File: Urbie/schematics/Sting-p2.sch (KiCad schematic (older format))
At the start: 12 parts

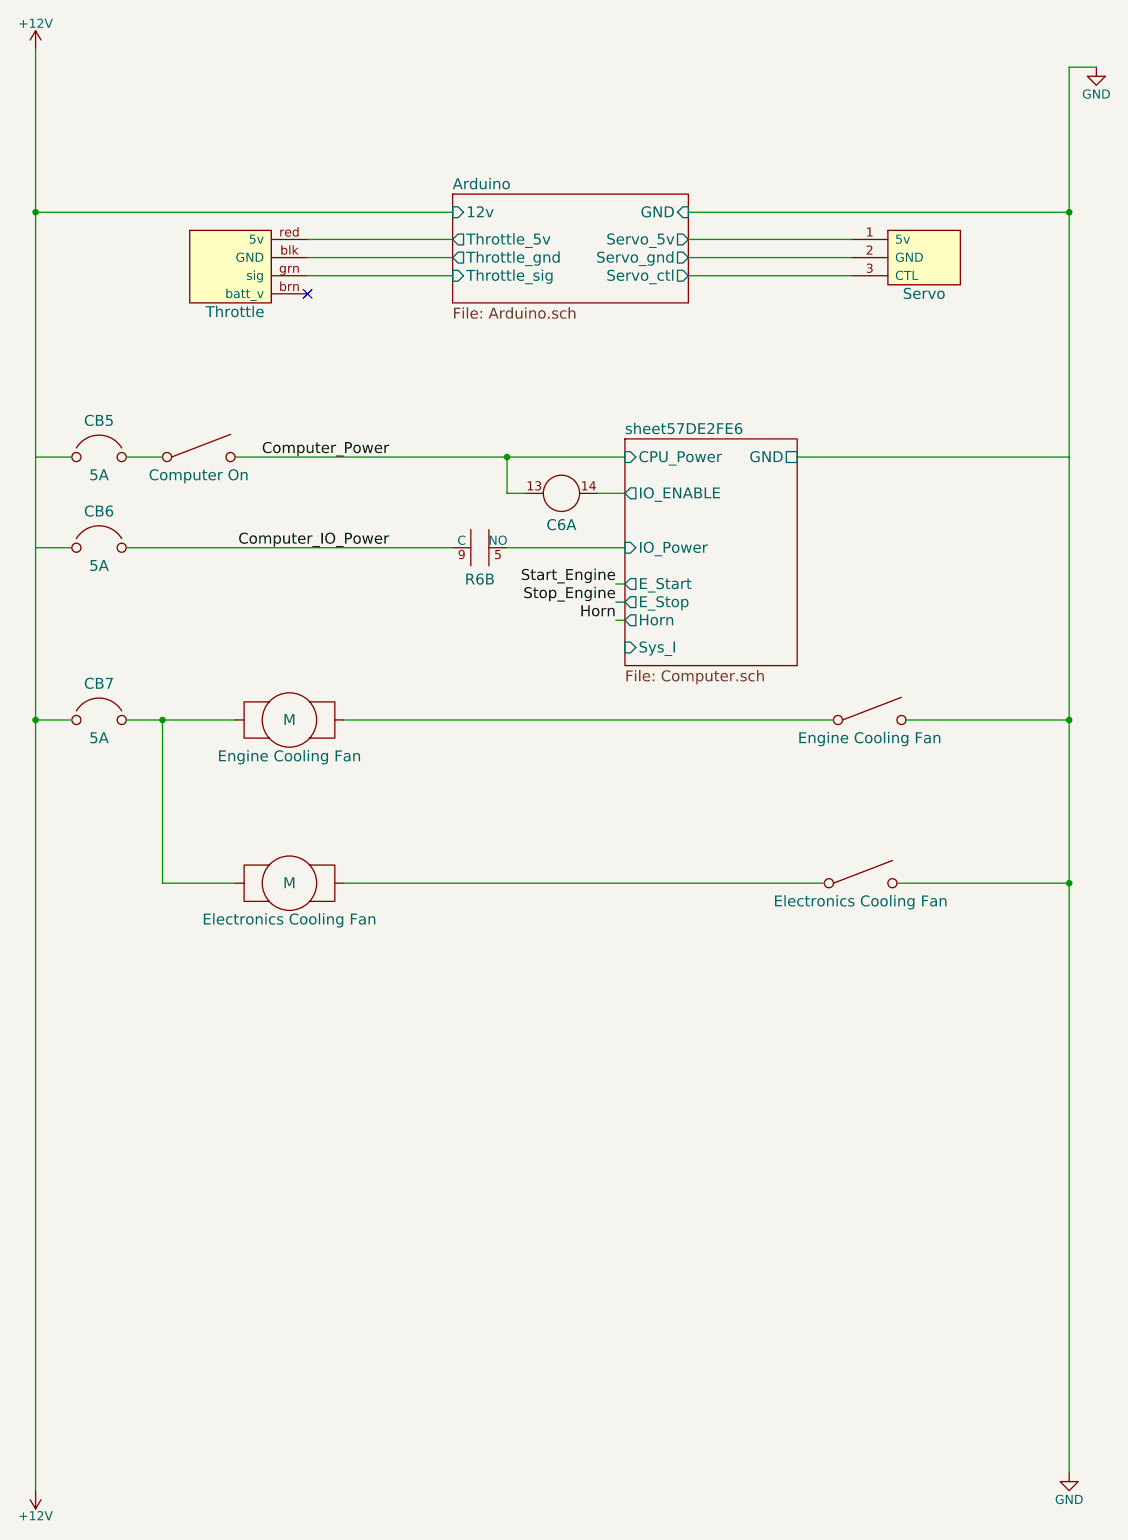
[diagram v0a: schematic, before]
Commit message: added DPDT switch for Hazard lights on Urbie
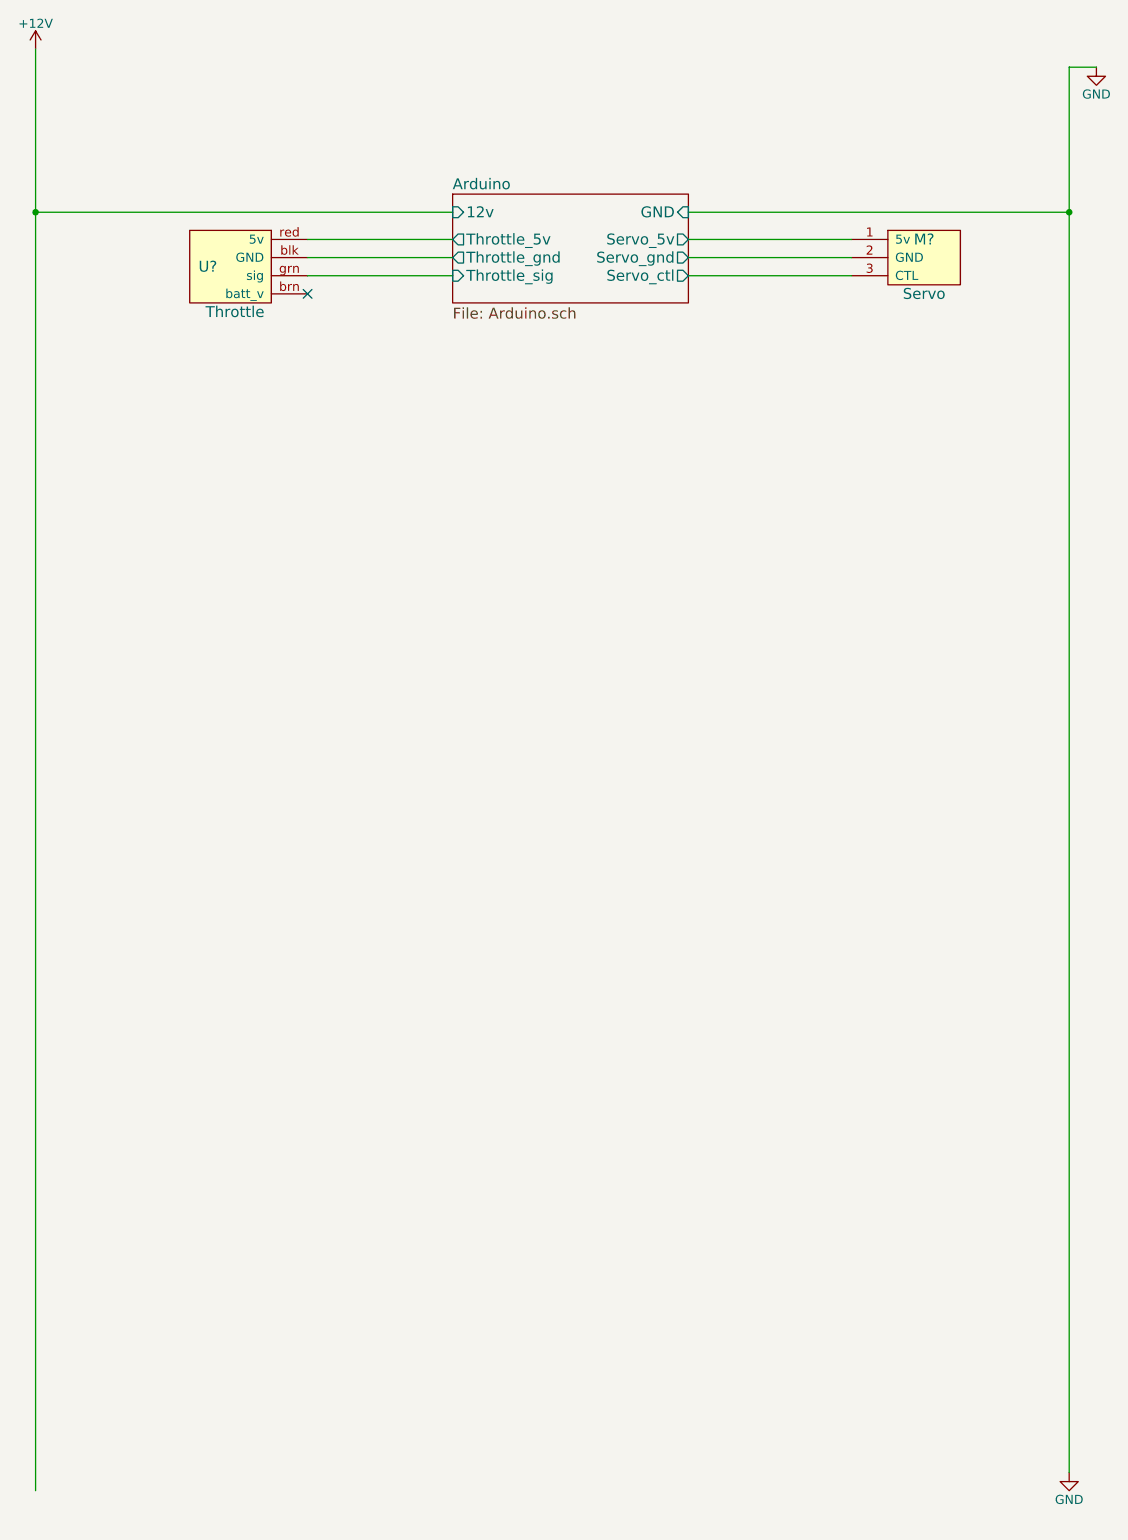
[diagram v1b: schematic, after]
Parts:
- removed C6, R6: CR, symbol CR
- removed CB5, CB6, CB7: 5A, symbol CB
- removed M: Engine Cooling Fan, symbol Motor
- removed M: Electronics Cooling Fan, symbol Motor
- removed SW?: Computer On, symbol SW_SPST
- removed SW?: Engine Cooling Fan, symbol SW_SPST
- removed SW?: Electronics Cooling Fan, symbol SW_SPST
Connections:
- net labels removed: Computer_IO_Power, Computer_Power, Horn, Start_Engine, Stop_Engine
- wire segments 32 -> 11
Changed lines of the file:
@@
 EESchema Schematic File Version 2
+LIBS:UrbieSchematics-rescue
 LIBS:power
 LIBS:device
@@
 $Descr USLetter 8500 11000 portrait
 encoding utf-8
-Sheet 3 6
-Title "Urbie - Gasoline Urban Concept"
-Date "2016-11-19"
-Rev "1.2"
+Sheet 4 5
+Title "Sting - Gasoline Prototype"
+Date "2016-08-01"
+Rev "1.0"
 Comp "Cedarville University"
-Comment1 "Tineka Witt"
-Comment2 "Page 2"
+Comment1 "Samuel Ellicott"
+Comment2 "Throttle"
 Comment3 ""
 Comment4 ""
@@
 	1    0    0    -1
 $EndComp
+Wire Wire Line
+	1400 900  1400 8850
+Wire Wire Line
+	7100 1000 7100 8750
 $Comp
 L GND #PWR?
@@
 	1    0    0    -1
 $EndComp
+Wire Wire Line
+	7100 1000 7250 1000
 $Comp
 L Servo M?
 U 1 1 57A231A6
 P 6300 2050
-F 0 "M?" H 6300 2150 60  0001 C CNN
+F 0 "M?" H 6300 2150 60  0000 C CNN
 F 1 "Servo" H 6300 1850 60  0000 C CNN
 F 2 "" H 6300 2050 60  0000 C CNN
@@
 	1    0    0    -1
 $EndComp
+Connection ~ 1400 1800
 $Sheet
 S 3700 1700 1300 600
@@
 F9 "Servo_ctl" O R 5000 2150 60
 $EndSheet
-$Comp
-L Throttle U?
-U 1 1 57A269DC
-P 2700 2100
-F 0 "U?" H 2350 2100 60  0001 C CNN
-F 1 "Throttle" H 2500 1850 60  0000 C CNN
-F 2 "" H 2700 2200 60  0000 C CNN
-F 3 "" H 2700 2200 60  0000 C CNN
-	1    2700 2100
-	1    0    0    -1
-$EndComp
-NoConn ~ 2900 2250
-Text Label 4600 3850 2    60   ~ 0
-Start_Engine
-Text Label 4600 3950 2    60   ~ 0
-Stop_Engine
-Text Label 4600 4050 2    60   ~ 0
-Horn
-Text Label 3350 3650 2    60   ~ 0
-Computer_IO_Power
-Text Label 3350 3150 2    60   ~ 0
-Computer_Power
-$Comp
-L CR CR?
-U 2 1 57DE2FF6
-P 3850 3650
-AR Path="/57DE2FF6" Ref="CR?"  Part="2"
-AR Path="/57A204AA/57DE2FF6" Ref="R6"  Part="2"
-F 0 "R6" H 3850 3475 60  0000 C CNN
-F 1 "CR" H 3850 3400 60  0001 C CNN
-F 2 "" H 3850 3650 60  0000 C CNN
-F 3 "" H 3850 3650 60  0000 C CNN
-	2    3850 3650
-	1    0    0    -1
-$EndComp
-$Comp
-L CR CR?
-U 1 1 57DE3001
-P 4300 3350
-AR Path="/57DE3001" Ref="CR?"  Part="1"
-AR Path="/57A204AA/57DE3001" Ref="C6"  Part="1"
-F 0 "C6" H 4300 3175 60  0000 C CNN
-F 1 "CR" H 4300 3350 60  0001 C CNN
-F 2 "" H 4300 3350 60  0000 C CNN
-F 3 "" H 4300 3350 60  0000 C CNN
-	1    4300 3350
-	1    0    0    -1
-$EndComp
-$Sheet
-S 4650 3050 950  1250
-U 57DE300F
-F0 "sheet57DE2FE6" 60
-F1 "Computer.sch" 60
-F2 "CPU_Power" I L 4650 3150 60
-F3 "IO_Power" I L 4650 3650 60
-F4 "GND" U R 5600 3150 60
-F5 "IO_ENABLE" O L 4650 3350 60
-F6 "E_Start" O L 4650 3850 60
-F7 "E_Stop" O L 4650 3950 60
-F8 "Horn" O L 4650 4050 60
-F9 "Sys_I" I L 4650 4200 60
-$EndSheet
-$Comp
-L SW_SPST SW?
-U 1 1 57DE3030
-P 2300 3150
-F 0 "SW?" H 2300 3300 60  0001 C CNN
-F 1 "Computer On" H 2300 3050 60  0000 C CNN
-F 2 "" H 2300 3150 60  0000 C CNN
-F 3 "" H 2300 3150 60  0000 C CNN
-	1    2300 3150
-	1    0    0    -1
-$EndComp
-$Comp
-L CB CB6
-U 1 1 57DE3037
-P 1750 3650
-F 0 "CB6" H 1750 3850 60  0000 C CNN
-F 1 "5A" H 1750 3550 60  0000 C CNN
-F 2 "" H 1750 3650 60  0000 C CNN
-F 3 "" H 1750 3650 60  0000 C CNN
-	1    1750 3650
-	1    0    0    -1
-$EndComp
-$Comp
-L CB CB5
-U 1 1 57DE303E
-P 1750 3150
-F 0 "CB5" H 1750 3350 60  0000 C CNN
-F 1 "5A" H 1750 3050 60  0000 C CNN
-F 2 "" H 1750 3150 60  0000 C CNN
-F 3 "" H 1750 3150 60  0000 C CNN
-	1    1750 3150
-	1    0    0    -1
-$EndComp
-$Comp
-L CB CB7
-U 1 1 57DF43A7
-P 1750 4600
-F 0 "CB7" H 1750 4800 60  0000 C CNN
-F 1 "5A" H 1750 4500 60  0000 C CNN
-F 2 "" H 1750 4600 60  0000 C CNN
-F 3 "" H 1750 4600 60  0000 C CNN
-	1    1750 4600
-	1    0    0    -1
-$EndComp
-Wire Wire Line
-	1400 900  1400 8850
-Wire Wire Line
-	7100 1000 7100 8750
-Wire Wire Line
-	7100 1000 7250 1000
-Connection ~ 1400 1800
 Wire Wire Line
 	5900 1950 5000 1950
@@
 Wire Wire Line
 	1400 1800 3700 1800
+$Comp
+L Throttle U?
+U 1 1 57A269DC
+P 2700 2100
+F 0 "U?" H 2350 2100 60  0000 C CNN
+F 1 "Throttle" H 2500 1850 60  0000 C CNN
+F 2 "" H 2700 2200 60  0000 C CNN
+F 3 "" H 2700 2200 60  0000 C CNN
+	1    2700 2100
+	1    0    0    -1
+$EndComp
 Wire Wire Line
 	2900 1950 3700 1950
@@
 Wire Wire Line
 	2900 2150 3700 2150
-Wire Wire Line
-	4600 4050 4650 4050
-Wire Wire Line
-	4600 3950 4650 3950
-Wire Wire Line
-	4600 3850 4650 3850
-Wire Wire Line
-	3700 3650 1900 3650
-Wire Wire Line
-	4000 3650 4650 3650
-Connection ~ 4000 3150
-Wire Wire Line
-	4000 3350 4000 3150
-Wire Wire Line
-	4100 3350 4000 3350
-Wire Wire Line
-	4500 3350 4650 3350
-Wire Wire Line
-	5600 3150 7100 3150
-Wire Wire Line
-	2500 3150 4650 3150
-Wire Wire Line
-	1900 3150 2100 3150
-Wire Wire Line
-	1600 3650 1400 3650
-Wire Wire Line
-	1600 3150 1400 3150
-Wire Wire Line
-	1600 4600 1400 4600
-Connection ~ 1400 4600
-$Comp
-L Motor M
-U 1 1 57DF484D
-P 2800 4600
-F 0 "M" H 2800 4600 60  0000 C CNN
-F 1 "Engine Cooling Fan" H 2800 4400 60  0000 C CNN
-F 2 "" H 2800 4600 60  0000 C CNN
-F 3 "" H 2800 4600 60  0000 C CNN
-	1    2800 4600
-	1    0    0    -1
-$EndComp
-$Comp
-L Motor M
-U 1 1 57DF4930
-P 2800 5500
-F 0 "M" H 2800 5500 60  0000 C CNN
-F 1 "Electronics Cooling Fan" H 2800 5300 60  0000 C CNN
-F 2 "" H 2800 5500 60  0000 C CNN
-F 3 "" H 2800 5500 60  0000 C CNN
-	1    2800 5500
-	1    0    0    -1
-$EndComp
-Wire Wire Line
-	1900 4600 2500 4600
-$Comp
-L SW_SPST SW?
-U 1 1 57DF535D
-P 6000 4600
-F 0 "SW?" H 6000 4750 60  0001 C CNN
-F 1 "Engine Cooling Fan" H 6000 4500 60  0000 C CNN
-F 2 "" H 6000 4600 60  0000 C CNN
-F 3 "" H 6000 4600 60  0000 C CNN
-	1    6000 4600
-	1    0    0    -1
-$EndComp
-$Comp
-L SW_SPST SW?
-U 1 1 57DF54B6
-P 5950 5500
-F 0 "SW?" H 5950 5650 60  0001 C CNN
-F 1 "Electronics Cooling Fan" H 5950 5400 60  0000 C CNN
-F 2 "" H 5950 5500 60  0000 C CNN
-F 3 "" H 5950 5500 60  0000 C CNN
-	1    5950 5500
-	1    0    0    -1
-$EndComp
-Wire Wire Line
-	2100 4600 2100 5500
-Wire Wire Line
-	2100 5500 2500 5500
-Connection ~ 2100 4600
-Wire Wire Line
-	3100 4600 5800 4600
-Wire Wire Line
-	6200 4600 7100 4600
-Connection ~ 7100 4600
-Wire Wire Line
-	3100 5500 5750 5500
-Wire Wire Line
-	6150 5500 7100 5500
-Connection ~ 7100 5500
-$Comp
-L +12V #PWR?
-U 1 1 58274825
-P 1400 8850
-F 0 "#PWR?" H 1400 8700 50  0001 C CNN
-F 1 "+12V" H 1400 8990 50  0000 C CNN
-F 2 "" H 1400 8850 50  0000 C CNN
-F 3 "" H 1400 8850 50  0000 C CNN
-	1    1400 8850
-	-1   0    0    1
-$EndComp
+NoConn ~ 2900 2250
 $EndSCHEMATC
